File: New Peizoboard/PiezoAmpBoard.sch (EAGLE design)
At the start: 99 parts, among them IC3 TL072D, IC5 TL072D, IC6 TL072D, IC7 TL072D, J1 RJ45, U1 ARDUINOR3-BPLACE, U2 MIC5219 3.3V, X1 22-23-2021, X2 22-23-2021

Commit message: add 2 question points
From PC
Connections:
- net GND5 renamed AGND
- new net RX: U$2.D0/TOUCH/MOSI1/RX1
- new net SCL: U$2.D3/SCL2/CAN0TX/PWM
- new net SDA: U$2.D4/SDA2/CAN0RX/PWM
- new net TX: U$2.D1/TOUCH/MISO1/TX1
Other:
- note added: "S2C"
- note added: "Serial"
- note added: "What's that for"
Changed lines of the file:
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@@
 <part name="SUPPLY77" library="supply2" deviceset="GND3" device=""/>
 <part name="SUPPLY78" library="supply2" deviceset="GND4" device=""/>
-<part name="SUPPLY79" library="supply2" deviceset="GND5" device=""/>
+<part name="SUPPLY79" library="supply2" deviceset="AGND" device=""/>
 <part name="R3" library="rcl" deviceset="R-EU_" device="R0603"/>
 <part name="R4" library="rcl" deviceset="R-EU_" device="R0603"/>
@@
 <part name="U$2" library="Teensy-3.6" deviceset="TEENSY-3.6_ONLY_HOLES" device=""/>
 <part name="SUPPLY80" library="supply2" deviceset="GND" device=""/>
-<part name="SUPPLY81" library="supply2" deviceset="GND5" device=""/>
+<part name="SUPPLY81" library="supply2" deviceset="AGND" device=""/>
 <part name="U2" library="SparkFun-PowerIC" deviceset="V_REG_MIC5219" device="3.3V" value="MIC5219 3.3V"/>
 <part name="SUPPLY82" library="supply2" deviceset="+9V" device=""/>
@@
 <text x="355.6" y="193.04" size="1.778" layer="91">Signal_3</text>
 <text x="355.6" y="195.58" size="1.778" layer="91">Signal_4</text>
+<text x="256.54" y="210.82" size="1.778" layer="91">Serial</text>
+<text x="256.54" y="203.2" size="1.778" layer="91">S2C</text>
+<text x="205.74" y="259.08" size="1.778" layer="91">What's that for</text>
+<text x="251.46" y="20.32" size="1.778" layer="91">What's that for</text>
 </plain>
 <instances>
@@
 <instance part="R2" gate="G$1" x="213.36" y="208.28"/>
 <instance part="U$2" gate="G$1" x="279.4" y="226.06"/>
-<instance part="SUPPLY80" gate="GND" x="264.16" y="210.82"/>
+<instance part="SUPPLY80" gate="GND" x="251.46" y="213.36"/>
 <instance part="SUPPLY81" gate="G$1" x="355.6" y="218.44"/>
 <instance part="U2" gate="G$1" x="312.42" y="86.36"/>
@@
 <segment>
 <pinref part="U$2" gate="G$1" pin="GND@1"/>
-<wire x1="271.78" y1="215.9" x2="264.16" y2="215.9" width="0.1524" layer="91"/>
-<wire x1="264.16" y1="215.9" x2="264.16" y2="213.36" width="0.1524" layer="91"/>
+<wire x1="271.78" y1="215.9" x2="251.46" y2="215.9" width="0.1524" layer="91"/>
 <pinref part="SUPPLY80" gate="GND" pin="GND"/>
 </segment>
@@
 </segment>
 </net>
-<net name="GND5" class="0">
+<net name="AGND" class="0">
 <segment>
 <pinref part="U$1" gate="G$1" pin="OUT"/>
@@
 <wire x1="220.98" y1="195.58" x2="218.44" y2="195.58" width="0.1524" layer="91"/>
 <wire x1="220.98" y1="208.28" x2="220.98" y2="195.58" width="0.1524" layer="91"/>
-<pinref part="SUPPLY79" gate="G$1" pin="GND5"/>
+<pinref part="SUPPLY79" gate="G$1" pin="AGND"/>
 <wire x1="220.98" y1="195.58" x2="220.98" y2="190.5" width="0.1524" layer="91"/>
 <junction x="220.98" y="195.58"/>
@@
 <wire x1="342.9" y1="213.36" x2="347.98" y2="213.36" width="0.1524" layer="91"/>
 <wire x1="347.98" y1="213.36" x2="347.98" y2="220.98" width="0.1524" layer="91"/>
-<pinref part="SUPPLY81" gate="G$1" pin="GND5"/>
+<pinref part="SUPPLY81" gate="G$1" pin="AGND"/>
 <wire x1="347.98" y1="220.98" x2="355.6" y2="220.98" width="0.1524" layer="91"/>
 </segment>
@@
 </segment>
 </net>
+<net name="RX" class="0">
+<segment>
+<pinref part="U$2" gate="G$1" pin="D0/TOUCH/MOSI1/RX1"/>
+<wire x1="271.78" y1="213.36" x2="261.62" y2="213.36" width="0.1524" layer="91"/>
+</segment>
+</net>
+<net name="TX" class="0">
+<segment>
+<pinref part="U$2" gate="G$1" pin="D1/TOUCH/MISO1/TX1"/>
+<wire x1="271.78" y1="210.82" x2="261.62" y2="210.82" width="0.1524" layer="91"/>
+</segment>
+</net>
+<net name="SCL" class="0">
+<segment>
+<pinref part="U$2" gate="G$1" pin="D3/SCL2/CAN0TX/PWM"/>
+<wire x1="271.78" y1="205.74" x2="261.62" y2="205.74" width="0.1524" layer="91"/>
+</segment>
+</net>
+<net name="SDA" class="0">
+<segment>
+<pinref part="U$2" gate="G$1" pin="D4/SDA2/CAN0RX/PWM"/>
+<wire x1="271.78" y1="203.2" x2="261.62" y2="203.2" width="0.1524" layer="91"/>
+</segment>
+</net>

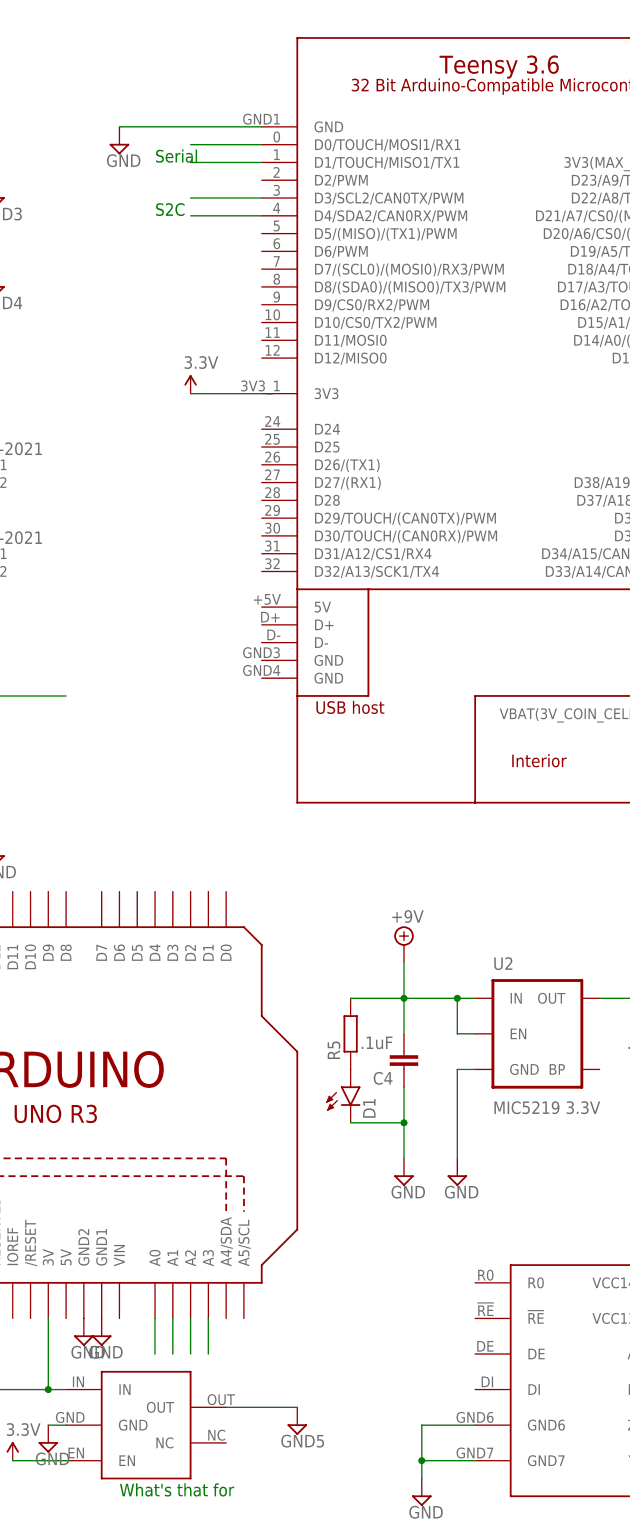
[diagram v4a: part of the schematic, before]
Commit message: Compelete the serial connection
From  PC
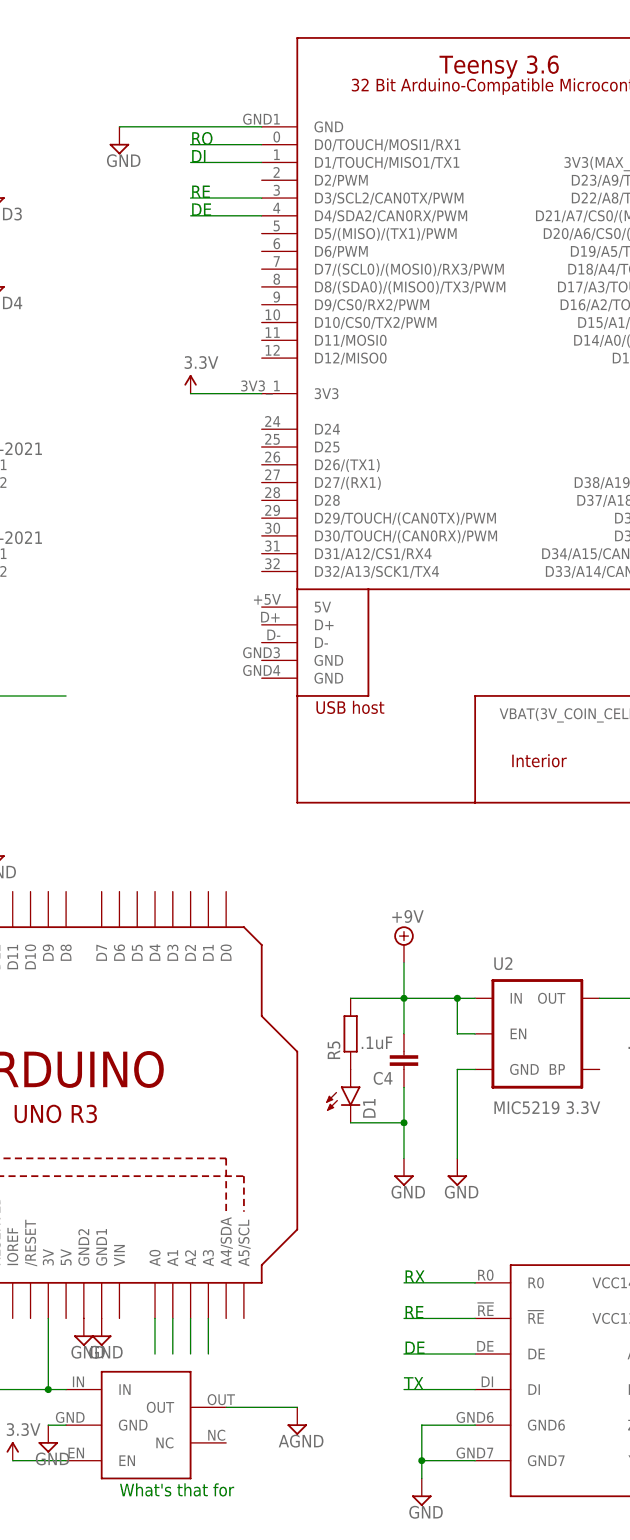
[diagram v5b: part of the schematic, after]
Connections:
- removed net SCL: U$2.D3/SCL2/CAN0TX/PWM
- removed net SDA: U$2.D4/SDA2/CAN0RX/PWM
- new net DE: U$3.DE
- new net RE: U$2.D3/SCL2/CAN0TX/PWM, U$2.D4/SDA2/CAN0RX/PWM, U$3.!RE
- net RX: now also U$3.R0
- net TX: now also U$3.DI
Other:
- note added: "DE"
- note added: "DI"
- note added: "RE"
- note added: "RO"
- note added: "RX"
- note added: "TX"
- note removed: "S2C"
- note removed: "Serial"
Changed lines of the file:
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@@
 <part name="SUPPLY39" library="supply2" deviceset="GND4" device=""/>
 <part name="SUPPLY40" library="supply2" deviceset="GND4" device=""/>
-<part name="SUPPLY74" library="supply2" deviceset="GND5" device=""/>
+<part name="SUPPLY74" library="supply2" deviceset="AGND" device=""/>
 <part name="SUPPLY75" library="supply2" deviceset="GND1" device=""/>
 <part name="SUPPLY76" library="supply2" deviceset="GND2" device=""/>
@@
 <text x="355.6" y="193.04" size="1.778" layer="91">Signal_3</text>
 <text x="355.6" y="195.58" size="1.778" layer="91">Signal_4</text>
-<text x="256.54" y="210.82" size="1.778" layer="91">Serial</text>
-<text x="256.54" y="203.2" size="1.778" layer="91">S2C</text>
 <text x="205.74" y="259.08" size="1.778" layer="91">What's that for</text>
 <text x="251.46" y="20.32" size="1.778" layer="91">What's that for</text>
+<text x="261.62" y="213.36" size="1.778" layer="91">RO</text>
+<text x="261.62" y="210.82" size="1.778" layer="91">DI</text>
+<text x="261.62" y="205.74" size="1.778" layer="91">RE</text>
+<text x="261.62" y="203.2" size="1.778" layer="91">DE</text>
+<text x="292.1" y="50.8" size="1.778" layer="91">RX</text>
+<text x="292.1" y="35.56" size="1.778" layer="91">TX</text>
+<text x="292.1" y="45.72" size="1.778" layer="91">RE</text>
+<text x="292.1" y="40.64" size="1.778" layer="91">DE</text>
 </plain>
 <instances>
@@
 <pinref part="U$1" gate="G$1" pin="OUT"/>
 <wire x1="266.7" y1="33.02" x2="276.86" y2="33.02" width="0.1524" layer="91"/>
-<pinref part="SUPPLY74" gate="G$1" pin="GND5"/>
+<pinref part="SUPPLY74" gate="G$1" pin="AGND"/>
 </segment>
 <segment>
@@
 <wire x1="271.78" y1="213.36" x2="261.62" y2="213.36" width="0.1524" layer="91"/>
 </segment>
+<segment>
+<pinref part="U$3" gate="G$1" pin="R0"/>
+<wire x1="302.26" y1="50.8" x2="292.1" y2="50.8" width="0.1524" layer="91"/>
+</segment>
 </net>
 <net name="TX" class="0">
@@
 <wire x1="271.78" y1="210.82" x2="261.62" y2="210.82" width="0.1524" layer="91"/>
 </segment>
-</net>
-<net name="SCL" class="0">
+<segment>
+<pinref part="U$3" gate="G$1" pin="DI"/>
+<wire x1="302.26" y1="35.56" x2="292.1" y2="35.56" width="0.1524" layer="91"/>
+</segment>
+</net>
+<net name="RE" class="0">
+<segment>
+<pinref part="U$3" gate="G$1" pin="!RE"/>
+<wire x1="302.26" y1="45.72" x2="292.1" y2="45.72" width="0.1524" layer="91"/>
+</segment>
 <segment>
 <pinref part="U$2" gate="G$1" pin="D3/SCL2/CAN0TX/PWM"/>
 <wire x1="271.78" y1="205.74" x2="261.62" y2="205.74" width="0.1524" layer="91"/>
 </segment>
-</net>
-<net name="SDA" class="0">
 <segment>
 <pinref part="U$2" gate="G$1" pin="D4/SDA2/CAN0RX/PWM"/>
@@
 </segment>
 </net>
+<net name="DE" class="0">
+<segment>
+<pinref part="U$3" gate="G$1" pin="DE"/>
+<wire x1="302.26" y1="40.64" x2="292.1" y2="40.64" width="0.1524" layer="91"/>
+</segment>
+</net>
